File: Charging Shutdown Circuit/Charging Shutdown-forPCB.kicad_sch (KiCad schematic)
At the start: 8 parts, among them J4 776087-1, SW1 SW-STOP, SW2 SH_RESET, U1 DK1A1B-12V

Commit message: charger stuff (don't break plz)
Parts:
- removed D5: D, Diode_SMD:D_2010_5025Metric_Pad1.52x2.65mm_HandSolder, symbol Device:D
- removed J4: 776087-1, 1FS_2_Global_Footprint_Library:TE_776087-1, symbol 1FS_2_Global_Symbol_Library:776087-1
- removed SW1: SW-STOP, Button_Switch_SMD:Nidec_Copal_CAS-120A, symbol Switch:SW_SPST
- removed SW2: SH_RESET, Button_Switch_SMD:Nidec_Copal_CAS-120A, symbol Switch:SW_SPST
- removed U1: DK1A1B-12V, 1FS_2_Global_Footprint_Library:RELAY_DK2A_PAN, symbol 2FS-1_Symbol Library:DK1A1B-12V
- added CR1: N-MOS, 1FS_2_Global_Footprint_Library:SO-8_STM, symbol 1FS_2_Global_Symbol_Library:STS6NF20V
- added J1: in charger, 1FS_2_Global_Footprint_Library:MOLEX_1053091202, symbol 1FS_2_Global_Symbol_Library:1053091202
- added J10: Button E-STOP, 1FS_2_Global_Footprint_Library:MOLEX_1053091202, symbol 1FS_2_Global_Symbol_Library:1053091202
- added J11: SH-RESET, 1FS_2_Global_Footprint_Library:MOLEX_1053091202, symbol 1FS_2_Global_Symbol_Library:1053091202
- added J13: TSMP (out), 1FS_2_Global_Footprint_Library:MOLEX_1053091202, symbol 1FS_2_Global_Symbol_Library:1053091202
- added J3: 120v DC (in), 1FS_2_Global_Footprint_Library:MOLEX_1053091202, symbol 1FS_2_Global_Symbol_Library:1053091202
- added J4: Out of Charger, 1FS_2_Global_Footprint_Library:MOLEX_1053091203, symbol 1FS_2_Global_Symbol_Library:1053091203
- added J6: Temp Sensor, 1FS_2_Global_Footprint_Library:MOLEX_1053091202, symbol 1FS_2_Global_Symbol_Library:1053091202
- added J7: AC in this world!, 1FS_2_Global_Footprint_Library:MOLEX_1053091202, symbol 1FS_2_Global_Symbol_Library:1053091202
- added J8: DC out of this world!, 1FS_2_Global_Footprint_Library:MOLEX_1053091202, symbol 1FS_2_Global_Symbol_Library:1053091202
- added K1: Charger Contactor +, 1FS_2_Global_Footprint_Library:GIGAVAC P115BDA, symbol 1FS_2_Global_Symbol_Library:GIGAVAC_P115BDA
- added K2: Charger Contactor -, 1FS_2_Global_Footprint_Library:GIGAVAC P115BDA, symbol 1FS_2_Global_Symbol_Library:GIGAVAC_P115BDA
- added R9 (x2): 5k, Resistor_SMD:R_0805_2012Metric_Pad1.20x1.40mm_HandSolder, symbol Device:R
- PS1: footprint (none) -> Converter_ACDC:Converter_ACDC_MeanWell_IRM-60-xx_THT
- R10, R9: footprint Resistor_SMD:R_0201_0603Metric -> Resistor_SMD:R_0805_2012Metric_Pad1.20x1.40mm_HandSolder
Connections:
- net +12V: now also J10.1, J11.2, J8.2
- net 120AC /L: now also J7.1
- net 120AC /N: now also J7.2
- net Charge_Enable: now also CR1.4 (G), J1.2
- net Charge_State: now also J4.2
- net GND: now also CR1.1 (S), CR1.2 (S), CR1.3 (S), J8.1, K1.3 (X1), K2.3 (X1)
- net SH_RESET: now also J11.1, J4.3
- net Shutdown_ACC_IN: now also J10.2, J4.1
- net Temperature Sensor: now also CR1.5 (D), CR1.6 (D), CR1.7 (D), CR1.8 (D), J6.2
- new net: J3.1, R9.1
- new net: J3.2, R9.1
- new net: J13.1, R9.2
- new net: J13.2, R9.2
- new net Shutdown_Final: J1.1, K1.4 (X2), K2.4 (X2)
- no-connect marks 15 -> 0
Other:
- note added: "LV"
- note added: "voltage divider"
- note removed: "12V"
- note removed: "3.3V"

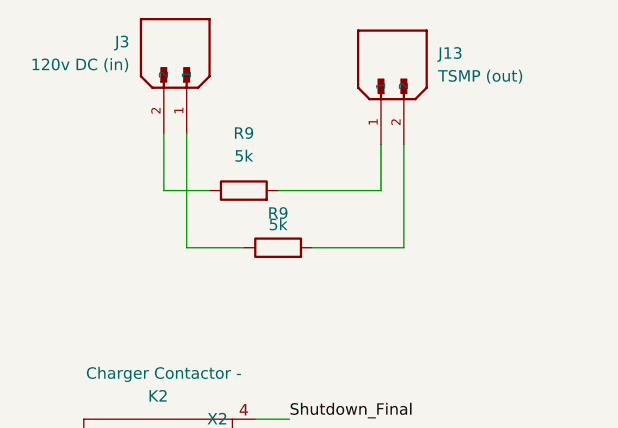
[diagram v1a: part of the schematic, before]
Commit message: fixing charger pcb from sam's comments
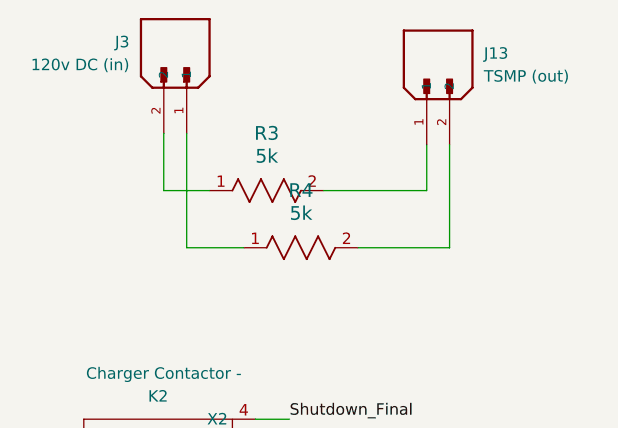
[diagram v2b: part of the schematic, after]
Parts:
- removed R9 (x2): 5k, Resistor_SMD:R_0805_2012Metric_Pad1.20x1.40mm_HandSolder, symbol Device:R
- added R3, R4: 5k, 1FS_2_Global_Footprint_Library:RES_WH&slash_NE_OHM, symbol 1FS_2_Global_Symbol_Library:WNE5K0FET
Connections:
- net at J3.1: now also R4.1
- net at J3.2: now also R3.1
- net at J13.1: now also R3.2
- net at J13.2: now also R4.2
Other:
- moved on the sheet: J13
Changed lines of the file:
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@@
     (stroke (width 0) (type default))
   )
-  (wire (pts (xy 217.17 44.45) (xy 227.33 44.45))
+  (wire (pts (xy 222.25 44.45) (xy 232.41 44.45))
     (stroke (width 0) (type default))
   )
@@
     (stroke (width 0) (type default))
   )
-  (wire (pts (xy 224.79 38.1) (xy 224.79 33.02))
+  (wire (pts (xy 229.87 38.1) (xy 229.87 33.02))
     (stroke (width 0) (type default))
   )
@@
     (stroke (width 0) (type default))
   )
-  (wire (pts (xy 213.36 38.1) (xy 224.79 38.1))
+  (wire (pts (xy 218.44 38.1) (xy 229.87 38.1))
     (stroke (width 0) (type default))
   )
@@
     (stroke (width 0) (type default))
   )
-  (wire (pts (xy 227.33 44.45) (xy 227.33 33.02))
+  (wire (pts (xy 232.41 44.45) (xy 232.41 33.02))
     (stroke (width 0) (type default))
   )
@@
         (path "/6367085a-e5be-41a6-9415-cc5003cc9235"
           (reference "J11") (unit 1)
+        )
+      )
+    )
+  )
+  (symbol (lib_id "1FS_2_Global_Symbol_Library:WNE5K0FET") (at 209.55 44.45 0) (unit 1)
+    (in_bom yes) (on_board yes) (dnp no) (fields_autoplaced)
+    (property "Reference" "R4" (at 215.9 38.1 0)
+      (effects (font (size 1.524 1.524)))
+    )
+    (property "Value" "5k" (at 215.9 40.64 0)
+      (effects (font (size 1.524 1.524)))
+    )
+    (property "Footprint" "1FS_2_Global_Footprint_Library:RES_WH&slash_NE_OHM" (at 209.55 36.83 0)
+      (effects (font (size 1.27 1.27) italic) hide)
+    )
+    (property "Datasheet" "WNE5K0FET" (at 208.28 40.64 0)
+      (effects (font (size 1.27 1.27) italic) hide)
+    )
+    (pin "1")
+    (pin "2")
+    (instances
+      (project "Charging Shutdown-forPCB"
+        (path "/6367085a-e5be-41a6-9415-cc5003cc9235"
+          (reference "R4") (unit 1)
         )
       )
@@
     )
   )
+  (symbol (lib_id "1FS_2_Global_Symbol_Library:WNE5K0FET") (at 205.74 38.1 0) (unit 1)
+    (in_bom yes) (on_board yes) (dnp no) (fields_autoplaced)
+    (property "Reference" "R3" (at 212.09 31.75 0)
+      (effects (font (size 1.524 1.524)))
+    )
+    (property "Value" "5k" (at 212.09 34.29 0)
+      (effects (font (size 1.524 1.524)))
+    )
+    (property "Footprint" "1FS_2_Global_Footprint_Library:RES_WH&slash_NE_OHM" (at 205.74 30.48 0)
+      (effects (font (size 1.27 1.27) italic) hide)
+    )
+    (property "Datasheet" "WNE5K0FET" (at 204.47 34.29 0)
+      (effects (font (size 1.27 1.27) italic) hide)
+    )
+    (pin "1")
+    (pin "2")
+    (instances
+      (project "Charging Shutdown-forPCB"
+        (path "/6367085a-e5be-41a6-9415-cc5003cc9235"
+          (reference "R3") (unit 1)
+        )
+      )
+    )
+  )
   (symbol (lib_id "1FS_2_Global_Symbol_Library:1053091202") (at 27.94 93.98 0) (unit 1)
     (in_bom yes) (on_board yes) (dnp no) (fields_autoplaced)
@@
         (path "/6367085a-e5be-41a6-9415-cc5003cc9235"
           (reference "#PWR010") (unit 1)
-        )
-      )
-    )
-  )
-  (symbol (lib_id "Device:R") (at 209.55 38.1 90) (unit 1)
-    (in_bom yes) (on_board yes) (dnp no) (fields_autoplaced)
-    (property "Reference" "R9" (at 209.55 31.75 90)
-      (effects (font (size 1.27 1.27)))
-    )
-    (property "Value" "5k" (at 209.55 34.29 90)
-      (effects (font (size 1.27 1.27)))
-    )
-    (property "Footprint" "Resistor_SMD:R_0805_2012Metric_Pad1.20x1.40mm_HandSolder" (at 209.55 39.878 90)
-      (effects (font (size 1.27 1.27)) hide)
-    )
-    (property "Datasheet" "~" (at 209.55 38.1 0)
-      (effects (font (size 1.27 1.27)) hide)
-    )
-    (pin "1")
-    (pin "2")
-    (instances
-      (project "Charging Shutdown Circuit"
-        (path "/160379ad-6194-4298-b157-948e3cc7f004"
-          (reference "R9") (unit 1)
-        )
-      )
-      (project "Charging Shutdown-forPCB"
-        (path "/6367085a-e5be-41a6-9415-cc5003cc9235"
-          (reference "R3") (unit 1)
         )
       )
@@
     )
   )
-  (symbol (lib_id "1FS_2_Global_Symbol_Library:1053091202") (at 224.79 27.94 90) (unit 1)
-    (in_bom yes) (on_board yes) (dnp no) (fields_autoplaced)
-    (property "Reference" "J13" (at 231.14 22.86 90)
+  (symbol (lib_id "1FS_2_Global_Symbol_Library:1053091202") (at 229.87 27.94 90) (unit 1)
+    (in_bom yes) (on_board yes) (dnp no) (fields_autoplaced)
+    (property "Reference" "J13" (at 236.22 22.86 90)
       (effects (font (size 1.27 1.27)) (justify right))
     )
-    (property "Value" "TSMP (out)" (at 231.14 25.4 90)
+    (property "Value" "TSMP (out)" (at 236.22 25.4 90)
       (effects (font (size 1.27 1.27)) (justify right))
     )
-    (property "Footprint" "1FS_2_Global_Footprint_Library:MOLEX_1053091202" (at 224.79 27.94 0)
-      (effects (font (size 1.27 1.27)) (justify bottom) hide)
-    )
-    (property "Datasheet" "" (at 224.79 27.94 0)
-      (effects (font (size 1.27 1.27)) hide)
-    )
-    (property "PARTREV" "H" (at 224.79 27.94 0)
-      (effects (font (size 1.27 1.27)) (justify bottom) hide)
-    )
-    (property "STANDARD" "Manufacturer Recommendations" (at 224.79 27.94 0)
-      (effects (font (size 1.27 1.27)) (justify bottom) hide)
-    )
-    (property "MAXIMUM_PACKAGE_HEIGHT" "10.51 mm" (at 224.79 27.94 0)
-      (effects (font (size 1.27 1.27)) (justify bottom) hide)
-    )
-    (property "MANUFACTURER" "Molex" (at 224.79 27.94 0)
+    (property "Footprint" "1FS_2_Global_Footprint_Library:MOLEX_1053091202" (at 229.87 27.94 0)
+      (effects (font (size 1.27 1.27)) (justify bottom) hide)
+    )
+    (property "Datasheet" "" (at 229.87 27.94 0)
+      (effects (font (size 1.27 1.27)) hide)
+    )
+    (property "PARTREV" "H" (at 229.87 27.94 0)
+      (effects (font (size 1.27 1.27)) (justify bottom) hide)
+    )
+    (property "STANDARD" "Manufacturer Recommendations" (at 229.87 27.94 0)
+      (effects (font (size 1.27 1.27)) (justify bottom) hide)
+    )
+    (property "MAXIMUM_PACKAGE_HEIGHT" "10.51 mm" (at 229.87 27.94 0)
+      (effects (font (size 1.27 1.27)) (justify bottom) hide)
+    )
+    (property "MANUFACTURER" "Molex" (at 229.87 27.94 0)
       (effects (font (size 1.27 1.27)) (justify bottom) hide)
     )
@@
         )
       )
-    )
-  )
-  (symbol (lib_id "Device:R") (at 213.36 44.45 90) (unit 1)
-    (in_bom yes) (on_board yes) (dnp no)
-    (property "Reference" "R9" (at 213.36 40.64 90)
-      (effects (font (size 1.27 1.27)))
-    )
-    (property "Value" "5k" (at 213.36 41.91 90)
-      (effects (font (size 1.27 1.27)))
-    )
-    (property "Footprint" "Resistor_SMD:R_0805_2012Metric_Pad1.20x1.40mm_HandSolder" (at 213.36 46.228 90)
-      (effects (font (size 1.27 1.27)) hide)
-    )
-    (property "Datasheet" "~" (at 213.36 44.45 0)
-      (effects (font (size 1.27 1.27)) hide)
-    )
-    (pin "1")
-    (pin "2")
-    (instances
-      (project "Charging Shutdown Circuit"
-        (path "/160379ad-6194-4298-b157-948e3cc7f004"
-          (reference "R9") (unit 1)
-        )
-      )
-      (project "Charging Shutdown-forPCB"
-        (path "/6367085a-e5be-41a6-9415-cc5003cc9235"
-          (reference "R4") (unit 1)
-        )
-      )
